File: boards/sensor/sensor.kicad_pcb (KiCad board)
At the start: 2 copper layers, 0 parts

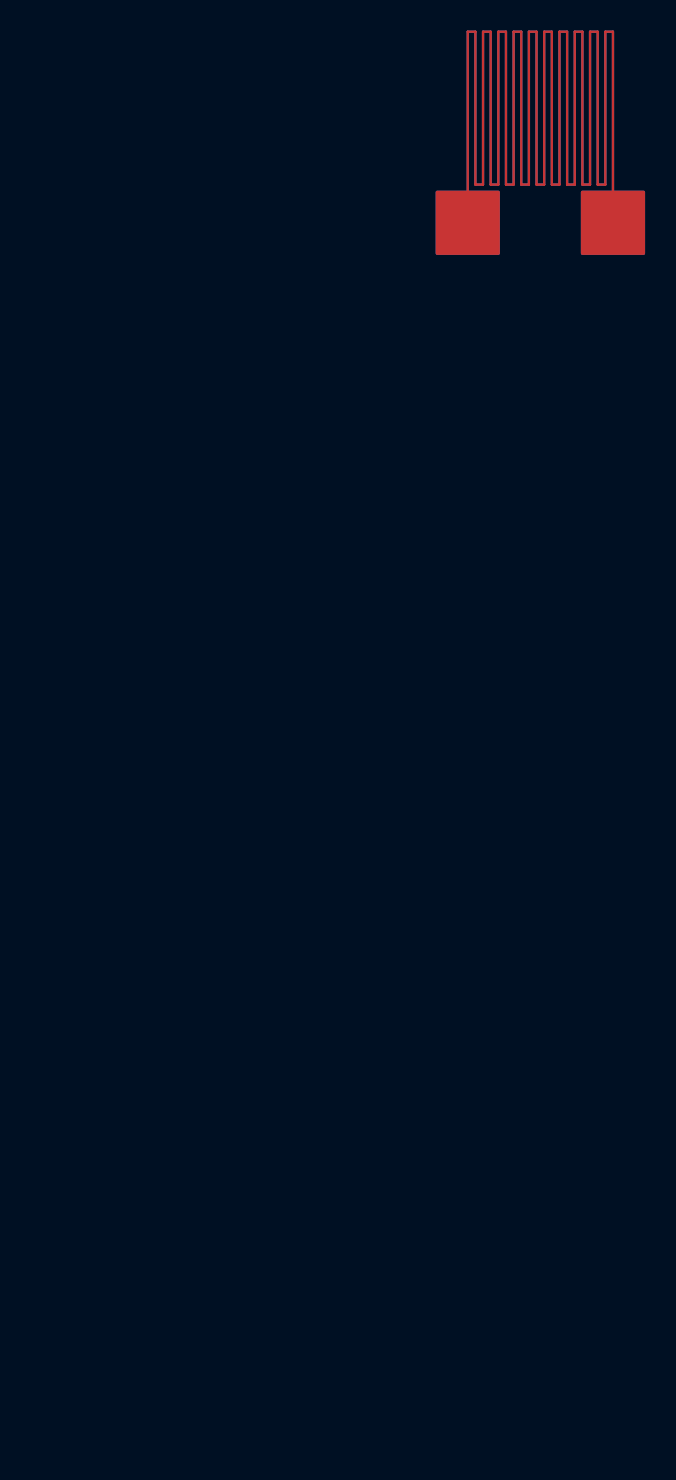
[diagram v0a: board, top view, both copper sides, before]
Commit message: boards/sensor: Change to thicker sensor
New sensor has longer leads, bigger pads, thicker traces and a larger sensing area (20x20mm instead of 10x10mm)

Signed-off-by: Philipp Macher <philipp-macher@web.de>
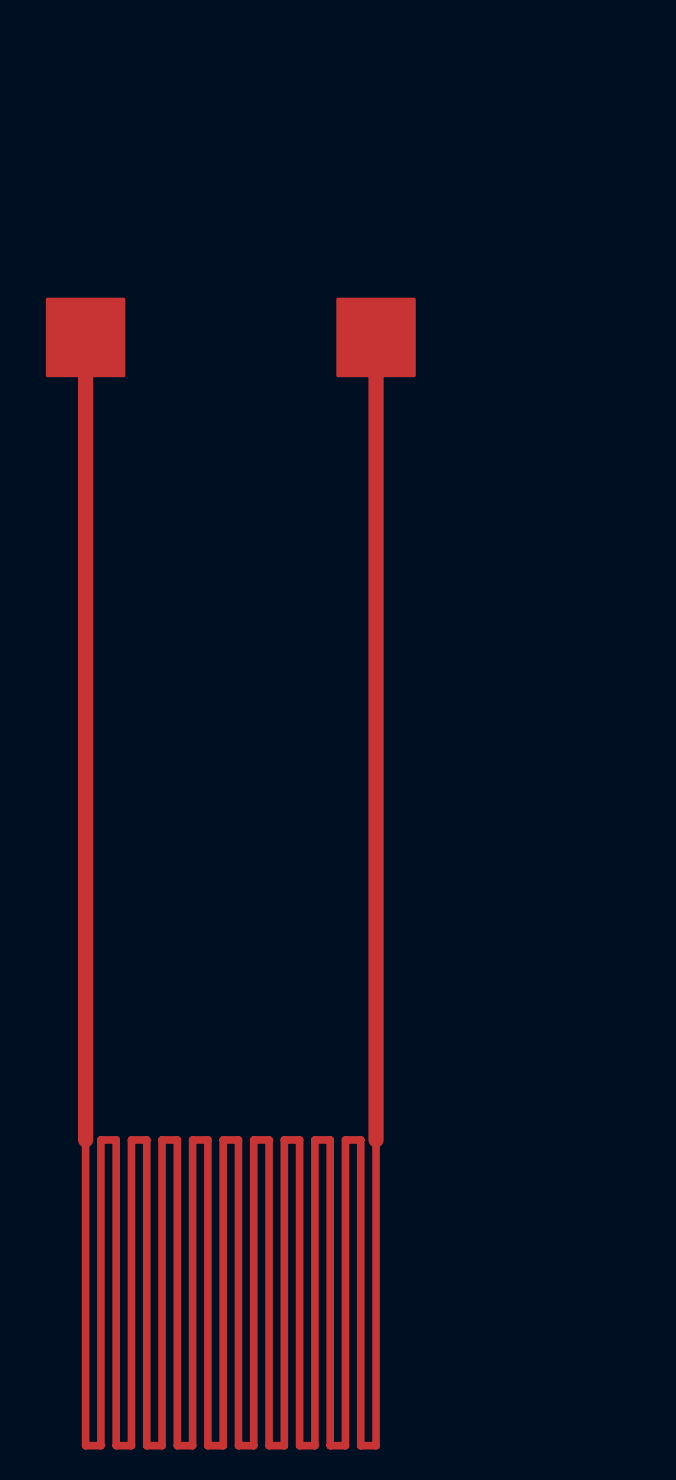
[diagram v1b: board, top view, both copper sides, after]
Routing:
- net (no net): track 0.00 -> 524.0 mm
- net sens: track 429.0 -> 0.00 mm

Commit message: More sensor work
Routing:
- net gnd: track 0.00 -> 526.8 mm
- net (no net): track 524.0 -> 0.00 mm

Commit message: Aktueller Stand
Signed-off-by: Philipp Macher <philipp-macher@web.de>
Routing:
- net gnd: track 526.8 -> 920.8 mm
